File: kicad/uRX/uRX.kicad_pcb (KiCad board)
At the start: 2 copper layers, 150 parts, among them J1 RF_AM_GND, J10 GPIO_A, J2 C165948, J4 Display, J6 U.FL, J9 RF_AM__In, Q1 BC847, SW1 RotaryEncoder_Switch, SW2 SW_DPDT_x2, SW3 Reset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

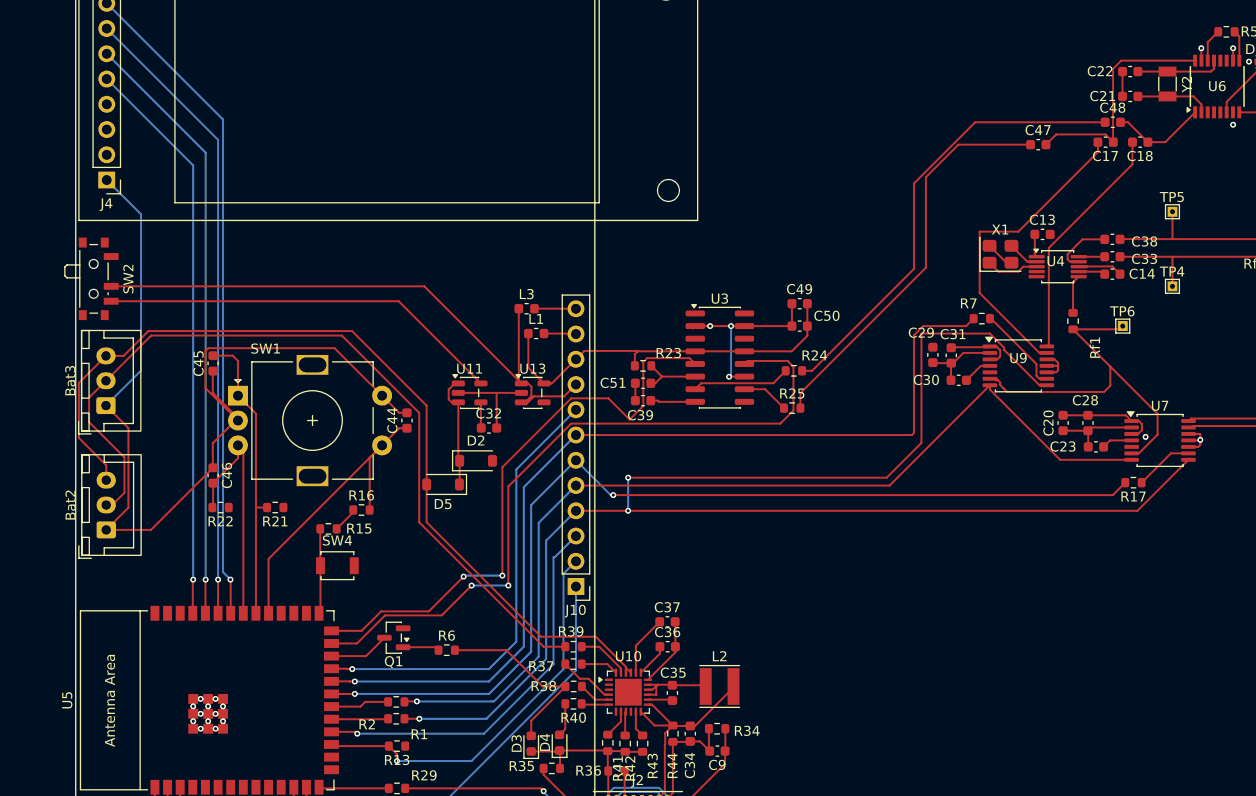
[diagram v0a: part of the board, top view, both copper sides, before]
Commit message: split stero-mono
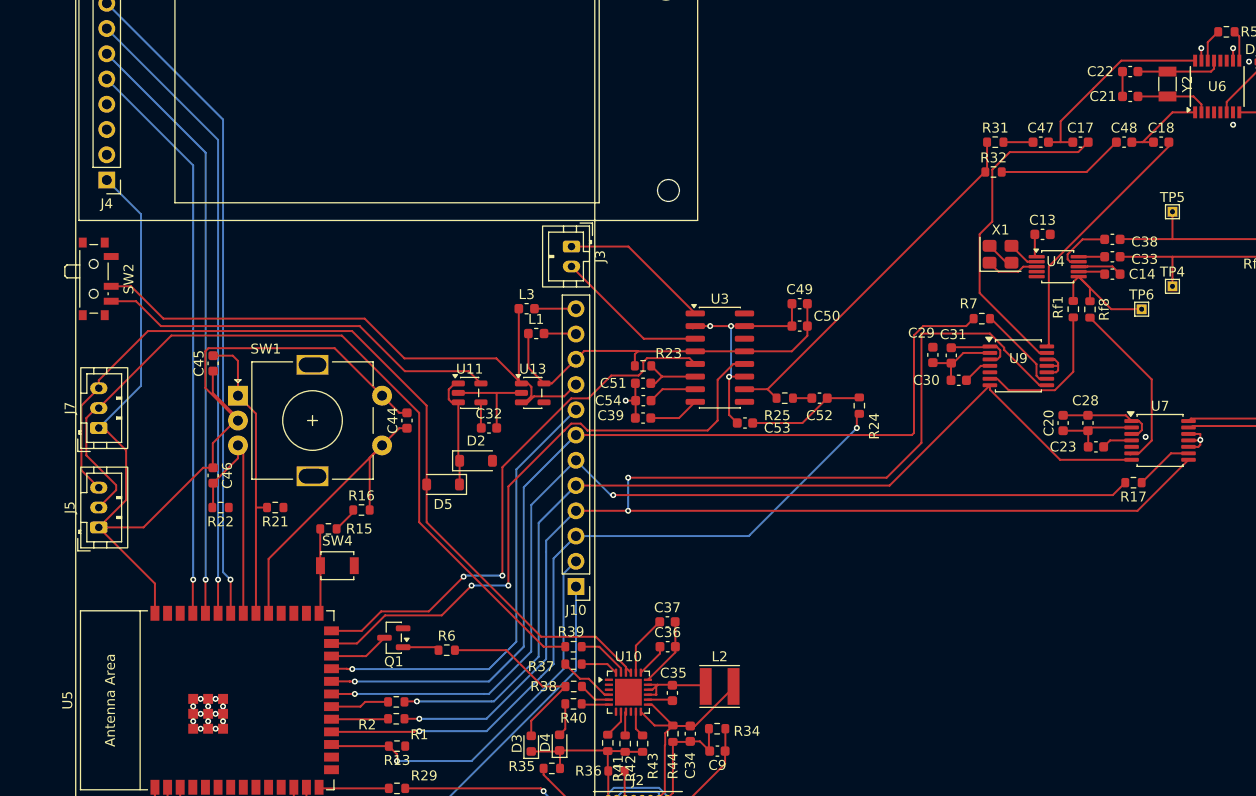
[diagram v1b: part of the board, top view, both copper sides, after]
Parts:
- removed Bat2, Bat3: JST-XH, Connector_JST:JST_XH_B3B-XH-A_1x03_P2.50mm_Vertical
- added C52: 1u, Capacitor_SMD:C_0603_1608Metric, F.Cu at (154.5, 89.2)
- added C53: 10n, Capacitor_SMD:C_0603_1608Metric, F.Cu at (147.0, 91.8)
- added C54: 1u, Capacitor_SMD:C_0603_1608Metric, F.Cu at (136.8, 89.5)
- added J3: Loudspeaker, Connector_JST:JST_PH_B2B-PH-K_1x02_P2.00mm_Vertical, F.Cu at (129.6, 74.0)
- added J5: BAT0, Connector_JST:JST_PH_B3B-PH-K_1x03_P2.00mm_Vertical, F.Cu at (82.0, 102.2)
- added J7: BAT1, Connector_JST:JST_PH_B3B-PH-K_1x03_P2.00mm_Vertical, F.Cu at (82.0, 92.2)
- added R31: 1k, Resistor_SMD:R_0603_1608Metric, F.Cu at (172.2, 63.5)
- added R32: 1k, Resistor_SMD:R_0603_1608Metric, F.Cu at (172.0, 66.5)
- added Rf8: 47, Resistor_SMD:R_0603_1608Metric, F.Cu at (181.7, 80.3)
- moved R24 7.45 mm to (158.5, 90.0), turned to -90 degrees
- moved TP6 2.55 mm to (186.9, 80.3)
- moved C17 2.53 mm to (180.8, 63.5), turned to 0 degrees
- moved C48 2.30 mm to (185.1, 63.5)
- moved C18 2.11 mm to (188.9, 63.5), turned to 0 degrees
- moved C39 1.75 mm to (136.8, 91.2)
- moved R25 1.25 mm to (151.0, 89.2)
- moved Rf1 1.20 mm to (180.0, 80.3), turned to -90 degrees
- moved C47 0.35 mm to (176.8, 63.5)
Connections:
- net Net-(U3-INR) renamed /AUDIO_MONO_4732
- C47 pad 1: /AUDIO_IN_R -> Net-(C47-Pad1)
- C48 pad 1: /AUDIO_IN_L -> Net-(C48-Pad1)
- J10 pad 3: ADC_SCKI -> /AUDIO_MONO_ESP
- R24 pad 1: Net-(U3-INL) -> Net-(C52-Pad1)
- R24 pad 2: /AUDIO_IN_L -> /AUDIO_MONO_ESP
- R25 pad 2: /AUDIO_IN_R -> Net-(C52-Pad2)
- Rf1 pad 1: ADC_SCKI -> Net-(U4-CLK2)
- Rf1 pad 2: Net-(U4-CLK2) -> ADC1_SCKI
- TP6 pad 1: ADC_SCKI -> Net-(U4-CLK2)
- U3 pad 1: /AUDIO_OUT_L+ -> Net-(J3-Pin_1)
- U3 pad 14: /AUDIO_OUT_R- -> unconnected-(U3--OUT_R-Pad14)
- U3 pad 16: /AUDIO_OUT_R+ -> unconnected-(U3-+OUT_R-Pad16)
- U3 pad 3: /AUDIO_OUT_L- -> Net-(J3-Pin_2)
- U5 pad 18: ADC_SCKI -> /AUDIO_MONO_ESP
- U7 pad 6: ADC_SCKI -> ADC0_SCKI
- U9 pad 6: ADC_SCKI -> ADC1_SCKI
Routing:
- net ADC_SCKI: track 77.7 -> 0.00 mm, vias 1 -> 0
- net /AUDIO_MONO_ESP: track 0.00 -> 73.3 mm, vias 0 -> 2
- net /AUDIO_IN_L: track 45.9 -> 0.00 mm
- net /AUDIO_IN_R: track 40.3 -> 0.00 mm
- net /AUDIO_MONO_4732: track 4.76 -> 37.6 mm
- net GND: track 286.0 -> 306.2 mm, vias 21 -> 22
- net ADC0_SCKI: track 0.00 -> 17.7 mm
- net Net-(J3-Pin_2): track 0.00 -> 15.5 mm
- net Net-(J3-Pin_1): track 0.00 -> 15.2 mm
- net ADC1_SCKI: track 0.00 -> 14.8 mm
- net Net-(C48-Pad1): track 0.00 -> 12.8 mm
- net Net-(C52-Pad1): track 0.00 -> 11.8 mm
- net /AUDIO_SHND: track 71.7 -> 62.0 mm
- net Net-(U4-CLK2): track 3.88 -> 13.3 mm
- net Net-(U3-INL): track 10.6 -> 5.70 mm
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
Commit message: clean-up pcb
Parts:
- moved C34 9.63 mm to (131.9, 123.6)
- moved R38 9.63 mm to (120.2, 118.8)
- moved R44 9.63 mm to (130.1, 123.6)
- moved U10 9.63 mm to (125.7, 119.4)
- moved J2 9.63 mm to (123.6, 130.1)
- moved R37 9.63 mm to (120.1, 116.6)
- moved R39 9.63 mm to (120.1, 114.8)
- moved R40 9.63 mm to (120.1, 120.6)
- moved C35 9.63 mm to (130.1, 119.5)
- moved C36 9.63 mm to (129.6, 114.8)
- moved C37 9.63 mm to (129.6, 112.3)
- moved C9 9.63 mm to (134.6, 125.3)
- moved L2 9.63 mm to (134.8, 118.8)
- moved R34 9.63 mm to (134.6, 123.1)
- moved R36 9.63 mm to (124.5, 127.3)
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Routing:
- net GND: track 306.2 -> 324.2 mm, vias 22 -> 23
- net USB_D-: track 25.8 -> 16.2 mm
- net USB_D+: track 27.9 -> 18.5 mm
- net Net-(D3-A): track 19.0 -> 11.1 mm
- net +VBatt: track 89.5 -> 83.4 mm
- net Net-(J5-Pin_2): track 82.0 -> 77.3 mm
- net Net-(J2-SHIELD): track 9.83 -> 13.2 mm
- net /AUDIO_MUTE: track 55.1 -> 52.9 mm
- net /AUDIO_SHND: track 62.0 -> 59.9 mm
- net Net-(Q1-B): track 3.69 -> 1.86 mm
- net Net-(J2-CC2): track 14.2 -> 13.5 mm

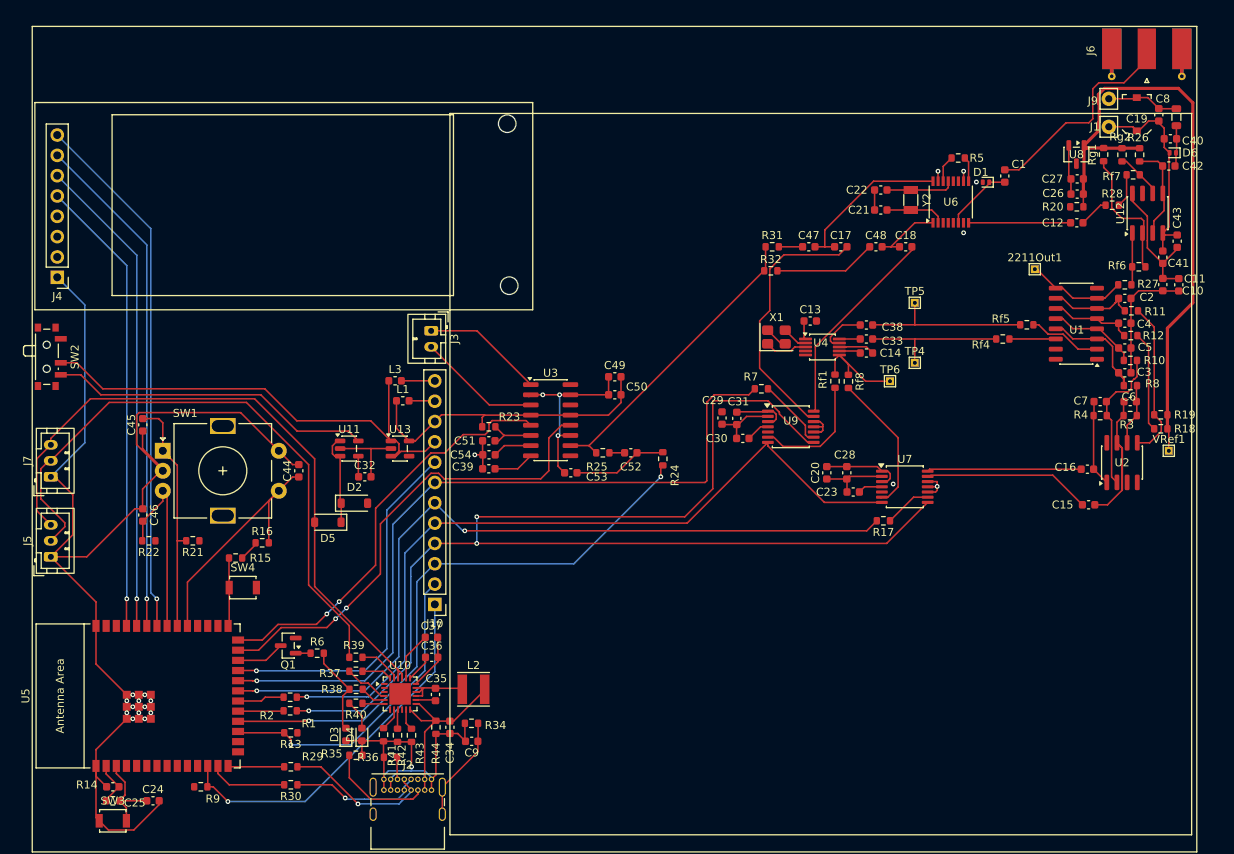
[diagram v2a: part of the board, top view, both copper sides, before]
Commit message: all lines connected
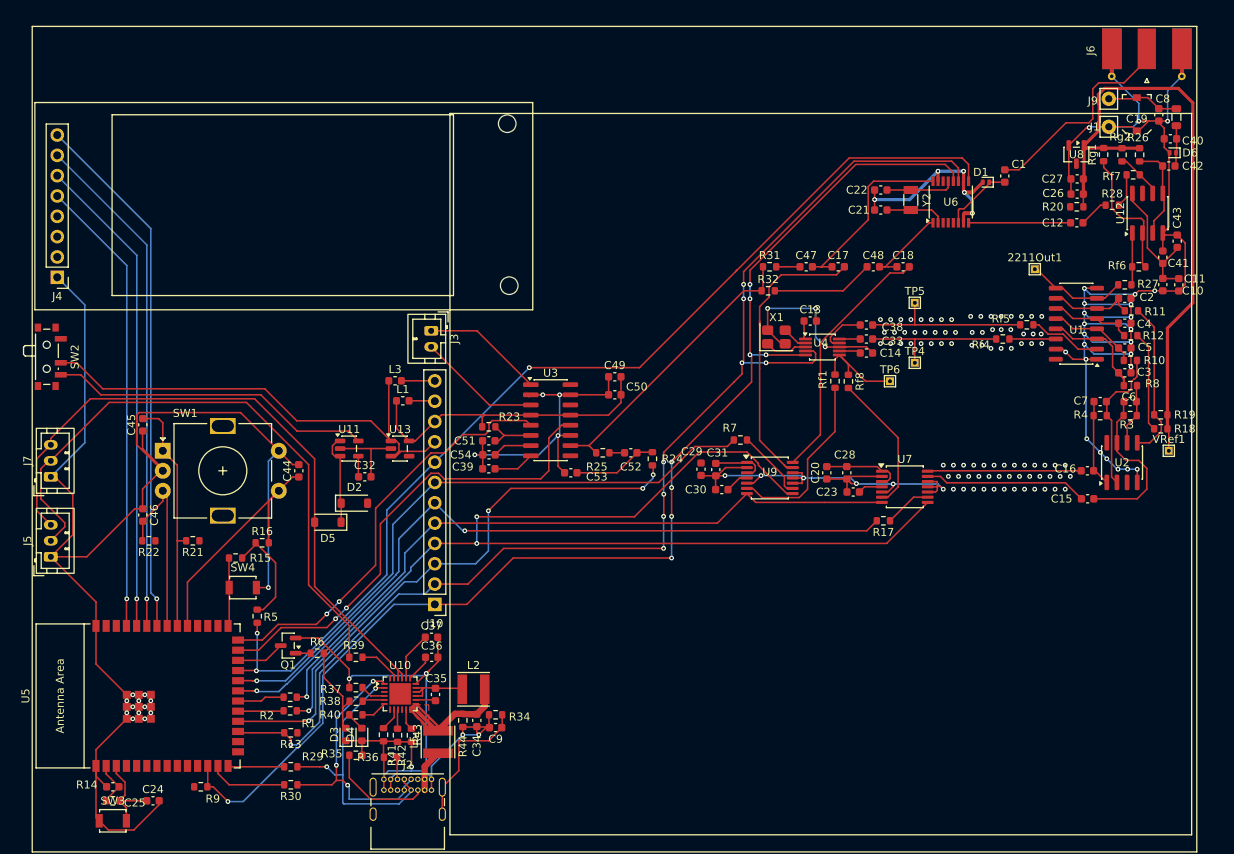
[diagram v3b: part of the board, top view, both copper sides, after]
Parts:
- added L5: L_Core_Ferrite, Inductor_SMD:L_Taiyo-Yuden_NR-40xx, F.Cu at (130.4, 125.4)
- added NT1: NetTie_2, NetTie:NetTie-2_SMD_Pad0.5mm, F.Cu at (196.7, 56.7)
- added NT2: NetTie_2, NetTie:NetTie-2_SMD_Pad0.5mm, F.Cu at (196.7, 59.3)
- moved R5 104.7 mm to (107.8, 109.7), turned to -90 degrees
- moved R7 6.92 mm to (168.2, 87.7)
- moved U9 6.92 mm to (171.9, 92.4)
- moved C29 6.92 mm to (163.3, 91.3)
- moved C30 6.92 mm to (165.9, 93.8)
- moved C31 6.92 mm to (165.1, 91.3)
- moved C34 3.47 mm to (135.2, 122.7)
- moved R44 3.47 mm to (133.5, 122.7)
- moved C9 3.44 mm to (137.6, 123.6)
- moved R34 3.19 mm to (137.6, 122.0)
- moved C18 2.52 mm to (188.5, 66.0)
- moved R31 2.52 mm to (171.8, 66.0)
- moved C17 2.52 mm to (180.4, 66.0)
- moved C47 2.52 mm to (176.4, 66.0)
- moved C48 2.52 mm to (184.8, 66.0)
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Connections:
- J2 pad A4: VBUS -> Net-(J2-VBUS-PadA4)
- J2 pad A9: VBUS -> Net-(J2-VBUS-PadA4)
- J2 pad B4: VBUS -> Net-(J2-VBUS-PadA4)
- J2 pad B9: VBUS -> Net-(J2-VBUS-PadA4)
- U10 pad 1: unconnected-(U10-DM-Pad1) -> USB_D-
- U10 pad 2: unconnected-(U10-DP-Pad2) -> USB_D+
- U2 pad 4: (no net) -> GND
- U2 pad 8: (no net) -> +5Vfiltered
- U6 pad 7: Earth -> Net-(U6-RFGND)
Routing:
- net GND: track 324.2 -> 562.0 mm, vias 23 -> 147
- net /SCL: track 39.6 -> 152.7 mm, vias 1 -> 9
- net /SDA: track 47.0 -> 157.0 mm, vias 1 -> 9
- net RST_4732: track 48.7 -> 131.4 mm, vias 1 -> 3
- net USB_D-: track 16.2 -> 33.3 mm, vias 1 -> 3
- net /I2S1_DOUT: track 94.9 -> 78.0 mm
- net /I2S_BCK: track 156.8 -> 141.1 mm
- net USB_D+: track 18.5 -> 34.1 mm, vias 1 -> 2
- net Net-(J2-VBUS-PadA4): track 0.00 -> 11.7 mm
- net /I2S_LRCK: track 97.6 -> 87.4 mm
- net ADC1_SCKI: track 14.8 -> 21.9 mm
- net VBUS: track 30.7 -> 23.7 mm
- net +3.3V: track 58.7 -> 65.3 mm
- net Net-(U9-VINR): track 25.6 -> 31.9 mm
- net /I2S0_DOUT: track 100.2 -> 94.1 mm
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- added copper zone on F.Cu, net VBUS

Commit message: work on power lines
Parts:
- removed J5: BAT0, Connector_JST:JST_PH_B3B-PH-K_1x03_P2.00mm_Vertical
- removed J7: BAT1, Connector_JST:JST_PH_B3B-PH-K_1x03_P2.00mm_Vertical
- added C55: 10u, Capacitor_SMD:C_0805_2012Metric, F.Cu at (135.1, 127.2)
- added C56: 10u, Capacitor_SMD:C_0805_2012Metric, F.Cu at (124.8, 115.0)
- added C57: 10u, Capacitor_SMD:C_0805_2012Metric, F.Cu at (121.0, 114.0)
- added J11: Bat1, Connector_JST:JST_PH_B2B-PH-K_1x02_P2.00mm_Vertical, F.Cu at (82.2, 98.0)
- added J8: Bat0, Connector_JST:JST_PH_B2B-PH-K_1x02_P2.00mm_Vertical, F.Cu at (82.2, 90.0)
- added L6: L_Core_Ferrite, Inductor_SMD:L_Taiyo-Yuden_NR-40xx, F.Cu at (124.2, 110.5)
- C34: footprint Capacitor_SMD:C_0603_1608Metric -> Capacitor_SMD:C_0805_2012Metric
- SW1: moved to B.Cu
- moved R39 10.0 mm to (112.8, 108.0), turned to 90 degrees
- moved D2 9.11 mm to (117.2, 104.2), turned to -90 degrees
- moved C45 5.40 mm to (98.8, 87.0)
- moved C46 5.28 mm to (98.8, 96.5)
- moved SW1 5.26 mm to (96.2, 94.2)
- moved C44 4.75 mm to (108.2, 91.5), turned to -90 degrees
- moved C37 1.72 mm to (129.2, 114.0)
- moved C9 1.32 mm to (138.8, 124.2)
- moved R34 1.18 mm to (138.8, 122.2)
- moved C36 1.01 mm to (129.2, 115.8)
- moved R44 0.80 mm to (133.5, 123.5)
- moved C34 0.74 mm to (135.8, 123.2)
- turned L5 to -90 degrees
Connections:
- C34 pad 1: VBUS -> VBUSfiltered
- C45 pad 2: Net-(U5-MTCK/GPIO39/CLK_OUT3/SUBSPICS1) -> Net-(U5-MTDO/GPIO40/CLK_OUT2)
- C46 pad 2: Net-(U5-MTDO/GPIO40/CLK_OUT2) -> Net-(U5-MTCK/GPIO39/CLK_OUT3/SUBSPICS1)
- D2 pad 2: VBUS -> VBUSfiltered
- J2 pad A4: Net-(J2-VBUS-PadA4) -> Net-(C55-Pad2)
- J2 pad A9: Net-(J2-VBUS-PadA4) -> Net-(C55-Pad2)
- J2 pad B4: Net-(J2-VBUS-PadA4) -> Net-(C55-Pad2)
- J2 pad B9: Net-(J2-VBUS-PadA4) -> Net-(C55-Pad2)
- L2 pad 2: VBUS -> VBUSfiltered
- L5 pad 1: Net-(J2-VBUS-PadA4) -> VBUSfiltered
- L5 pad 2: VBUS -> Net-(C55-Pad2)
- R44 pad 1: VBUS -> VBUSfiltered
- U10 pad 12: VBUS -> VBUSfiltered
- U10 pad 13: VBUS -> VBUSfiltered
- U10 pad 21: +VBatt -> Net-(C56-Pad2)
- U10 pad 22: +VBatt -> Net-(C56-Pad2)
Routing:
- net VBUSfiltered: track 0.00 -> 42.7 mm
- net GND: track 562.0 -> 525.7 mm, vias 147 -> 154
- net VBUS: track 23.7 -> 0.00 mm
- net Net-(J11-Pin_2): track 77.0 -> 60.0 mm
- net Net-(C55-Pad2): track 0.00 -> 15.6 mm
- net +VBatt: track 83.4 -> 70.9 mm
- net Net-(U10-VBATM): track 5.28 -> 17.3 mm
- net Net-(J2-VBUS-PadA4): track 11.7 -> 0.00 mm
- net Net-(D2-K): track 11.0 -> 22.7 mm
- net Net-(U5-MTCK/GPIO39/CLK_OUT3/SUBSPICS1): track 30.0 -> 18.9 mm
- net Net-(C56-Pad2): track 0.00 -> 10.5 mm
- net Net-(U5-MTDO/GPIO40/CLK_OUT2): track 23.6 -> 28.3 mm
- net Net-(U5-GPIO38/FSPIWP/SUBSPIWP): track 31.9 -> 35.1 mm
- net Net-(C37-Pad1): track 6.11 -> 4.28 mm
- net Net-(C36-Pad1): track 3.41 -> 2.32 mm
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- removed copper zone on F.Cu, net VBUS

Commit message: seafile corruption
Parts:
- added L7: Ferrite_perl, Inductor_SMD:L_0603_1608Metric, F.Cu at (155.0, 75.0)
- moved R5 107.1 mm to (198.5, 52.8)
- moved L3 59.4 mm to (176.7, 51.0)
- moved L1 58.2 mm to (176.8, 54.2)
- moved R39 9.02 mm to (119.2, 114.2)
- moved R22 8.56 mm to (93.2, 91.8), turned to 0 degrees
- moved R6 5.32 mm to (117.2, 119.2), turned to -90 degrees
- moved 2211Out1 1.57 mm to (206.5, 66.8)
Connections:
- C10 pad 1: +5Vfiltered -> +5VfilteredQ
- C11 pad 1: +5Vfiltered -> +5VfilteredQ
- C20 pad 2: +5Vfiltered -> +5VfilteredM
- C23 pad 2: +3.3Vfiltered -> +3.3VfilteredM
- C28 pad 2: +5Vfiltered -> +5VfilteredM
- C29 pad 2: +5V -> +5VfilteredM
- C30 pad 2: +3.3V -> +3.3VfilteredM
- C31 pad 2: +5V -> +5VfilteredM
- C41 pad 1: +5Vfiltered -> +5VfilteredQ
- C43 pad 1: +5Vfiltered -> +5VfilteredQ
- J10 pad 11: +3.3Vfiltered -> unconnected-(J10-Pin_11-Pad11)
- J10 pad 12: +5Vfiltered -> unconnected-(J10-Pin_12-Pad12)
- L1 pad 2: +3.3Vfiltered -> +3.3VfilteredM
- L3 pad 2: +5Vfiltered -> +5VfilteredQ
- R20 pad 2: +5Vfiltered -> +5VfilteredQ
- R5 pad 1: +3.3V -> +3.3VfilteredM
- U1 pad 16: +5Vfiltered -> +5VfilteredQ
- U12 pad 8: +5Vfiltered -> +5VfilteredQ
- U2 pad 8: +5Vfiltered -> +5VfilteredQ
- U6 pad 14: +3.3V -> +3.3VfilteredM
- U7 pad 1: +5Vfiltered -> +5VfilteredM
- U7 pad 3: +5Vfiltered -> +5VfilteredM
- U7 pad 4: +3.3Vfiltered -> +3.3VfilteredM
- U9 pad 1: +5V -> +5VfilteredM
- U9 pad 3: +5V -> +5VfilteredM
- U9 pad 4: +3.3V -> +3.3VfilteredM
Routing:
- net +3.3V: track 65.3 -> 284.3 mm, vias 0 -> 12
- net +3.3VfilteredM: track 0.00 -> 120.8 mm, vias 0 -> 10
- net +5VfilteredQ: track 0.00 -> 106.3 mm, vias 0 -> 8
- net /SDA: track 157.0 -> 239.1 mm, vias 9 -> 11
- net /SCL: track 152.7 -> 234.0 mm, vias 9 -> 11
- net GND: track 525.7 -> 596.6 mm, vias 154 -> 155
- net +5V: track 68.7 -> 132.5 mm, vias 0 -> 1
- net +5VfilteredM: track 0.00 -> 47.5 mm, vias 0 -> 6
- net +5Vfiltered: track 32.2 -> 0.00 mm
- net Net-(U10-VBATM): track 17.3 -> 6.89 mm
- net Net-(J11-Pin_2): track 60.0 -> 68.9 mm
- net Net-(D3-A): track 11.2 -> 4.85 mm
- net +3.3Vfiltered: track 6.24 -> 0.00 mm
- net Net-(Q1-B): track 1.86 -> 6.35 mm
- net VBUSfiltered: track 42.7 -> 40.4 mm
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
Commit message: correct taylo
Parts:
- added JP1: AudioMix, Connector_PinHeader_2.54mm:PinHeader_1x02_P2.54mm_Vertical, F.Cu at (155.8, 86.0)
- C2, C3, C4: value 220n -> 470n
- C5: value 220n -> 470
- C6, C7: value 1.2n -> 5.6n
- R10, R11, R12, R8: value 1k -> 100
- R18, R19, R3, R4: value 47k -> 10k
- moved R8 7.12 mm to (219.5, 74.2)
- moved C3 5.05 mm to (216.1, 74.2)
- moved R18 4.62 mm to (223.0, 82.2)
- moved R19 4.62 mm to (223.0, 80.5)
- moved C15 3.45 mm to (214.1, 92.6)
- moved VRef1 3.45 mm to (224.2, 86.6)
- moved C6 3.45 mm to (219.4, 80.5)
- moved C7 3.45 mm to (215.7, 80.5)
- moved R3 3.45 mm to (219.4, 82.2)
- moved R4 3.45 mm to (215.7, 82.2)
- moved U2 3.45 mm to (218.4, 88.1)
- moved R12 3.20 mm to (219.5, 72.6)
- moved R10 3.18 mm to (219.5, 75.8)
- moved C16 2.63 mm to (214.1, 90.6)
- moved R11 2.48 mm to (219.5, 71.0)
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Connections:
- C3 pad 1: Net-(U1-1B4) -> Net-(U1-1B3)
- C5 pad 1: Net-(U1-1B3) -> Net-(U1-1B4)
- R10 pad 2: Net-(U1-1B3) -> Net-(U1-1B4)
- R25 pad 1: /AUDIO_MONO_4732 -> Net-(JP1-A)
- R8 pad 2: Net-(U1-1B4) -> Net-(U1-1B3)
- U3 pad 1: Net-(J3-Pin_1) -> unconnected-(U3-+OUT_L-Pad1)
- U3 pad 10: /AUDIO_MONO_4732 -> Net-(JP1-A)
- U3 pad 14: unconnected-(U3--OUT_R-Pad14) -> Net-(J3-Pin_2)
- U3 pad 16: unconnected-(U3-+OUT_R-Pad16) -> Net-(J3-Pin_1)
- U3 pad 3: Net-(J3-Pin_2) -> unconnected-(U3--OUT_L-Pad3)
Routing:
- net Net-(JP1-A): track 0.00 -> 15.7 mm
- net GND: track 596.6 -> 581.5 mm, vias 155 -> 146
- net /AUDIO_MONO_4732: track 36.0 -> 24.8 mm
- net Net-(U2A-+): track 12.5 -> 20.7 mm
- net Net-(J3-Pin_1): track 14.5 -> 20.2 mm
- net Net-(J3-Pin_2): track 14.7 -> 20.4 mm
- net Net-(U2B--): track 7.77 -> 13.0 mm
- net Net-(C15-Pad1): track 20.8 -> 16.0 mm
- net +3.3V: track 284.3 -> 288.8 mm
- net Net-(U7-VINR): track 19.1 -> 22.0 mm
- net Net-(U1-1B4): track 15.3 -> 12.8 mm
- net Net-(U1-1B2): track 10.5 -> 12.3 mm
- net Net-(U7-VINL): track 20.4 -> 22.2 mm
- net /VRev2.5: track 79.3 -> 77.6 mm
- net Net-(U1-1B3): track 10.9 -> 12.4 mm
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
